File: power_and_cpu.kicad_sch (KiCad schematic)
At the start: 83 parts, among them J1 USB_C_Receptacle_USB2.0, J2 Conn_01x05, J3 Conn_01x05, J4 Conn_01x04, J5 Conn_01x04, J6 Conn_01x03, SW1 SW_MEC_5G, U11 RP2040, U13 ADC081S021CISD/NOPB, U14 ADC081S021CISD/NOPB, U15 ADC081S021CISD/NOPB, U16 ADC081S021CISD/NOPB, U6 NCP1117-3.3_SOT223, U7 XL7045, U9 W25Q16JVSSIQ, Y1 Crystal_GND24

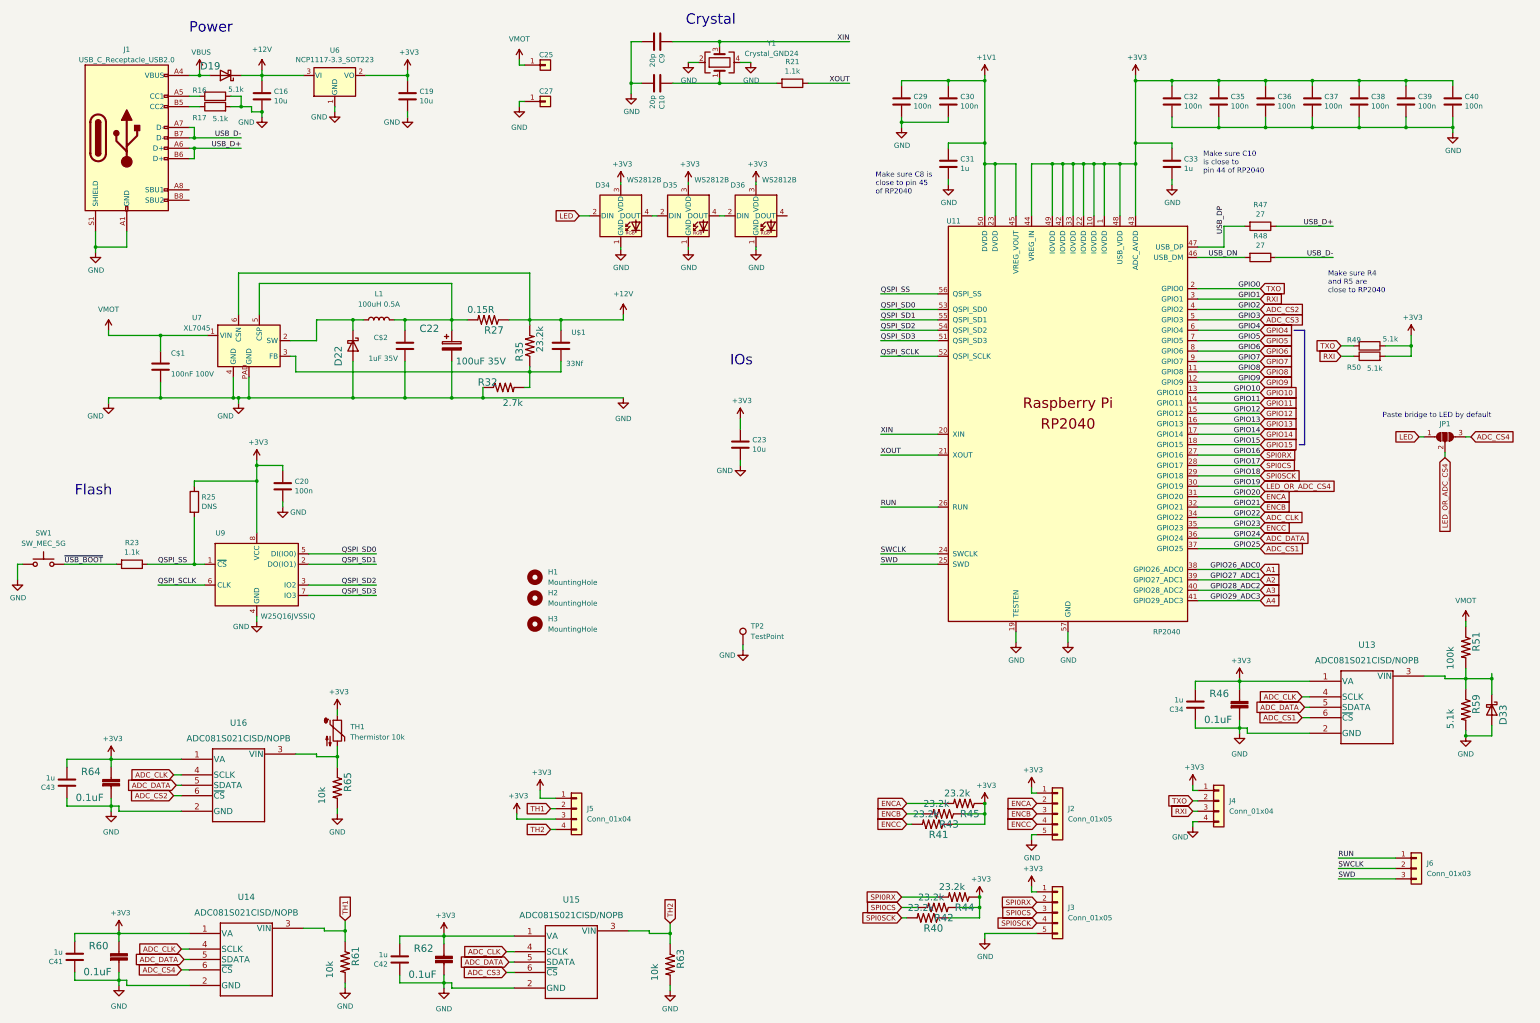
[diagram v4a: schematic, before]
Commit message: Additional updates to clean up power and capacitance on buck circuit.
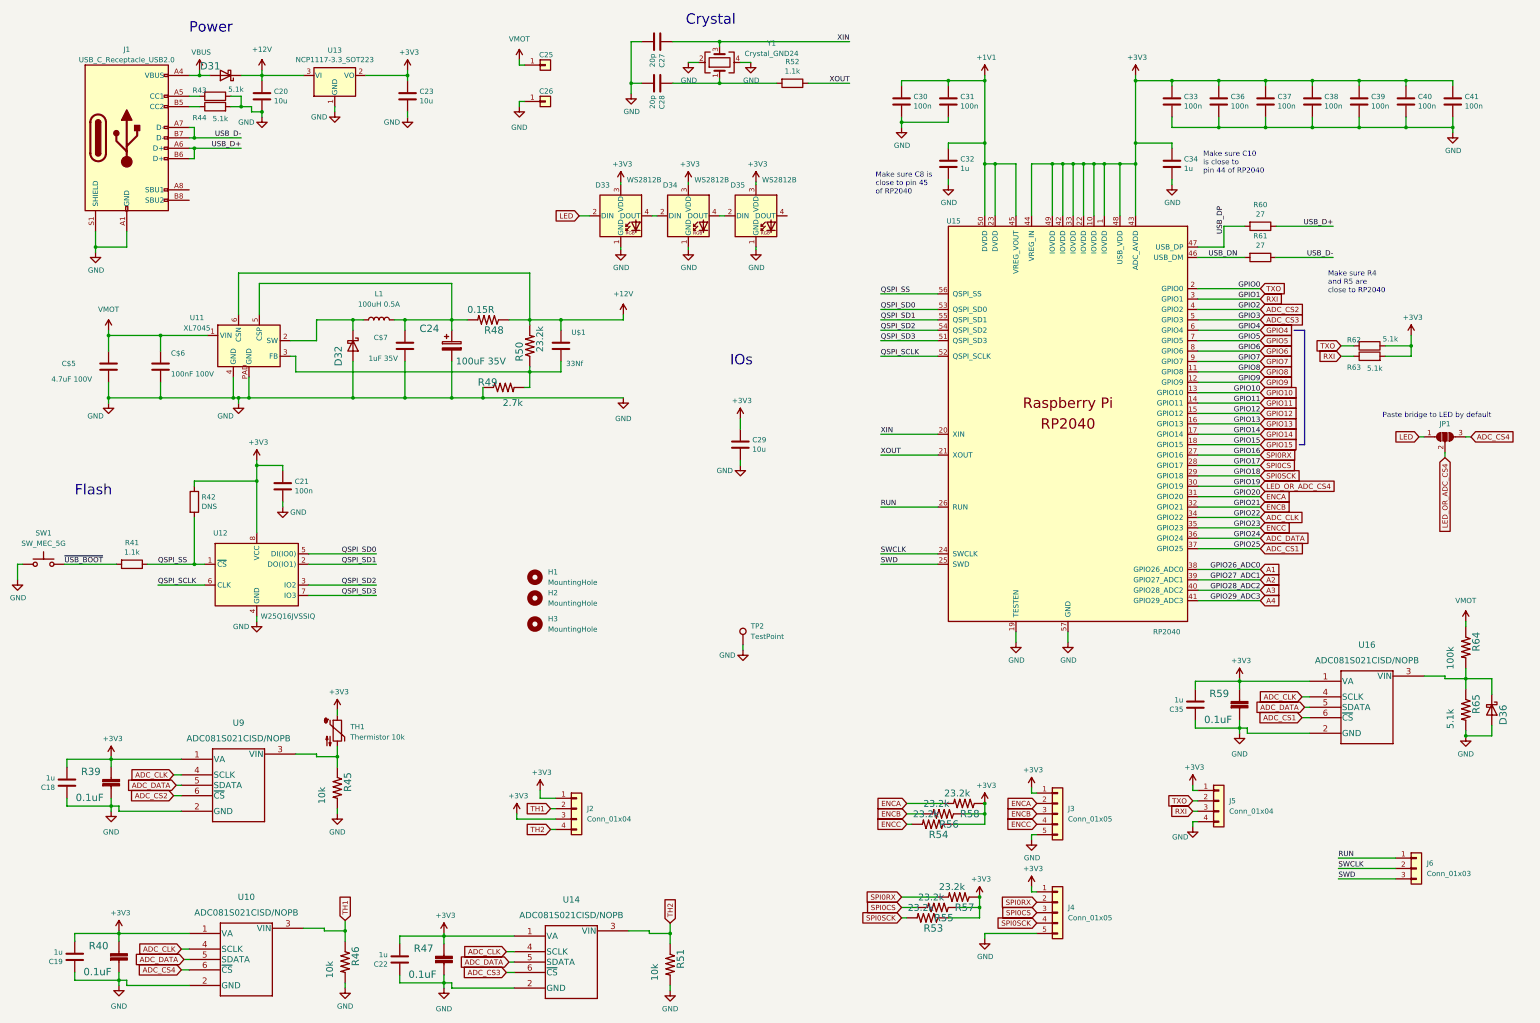
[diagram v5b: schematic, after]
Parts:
- added C$5: 4.7uF 100V, Capacitor_SMD:C_1210_3225Metric, symbol Device:C
- SW1: footprint Button_Switch_THT:SW_PUSH_6mm_H4.3mm -> parts:SW_TS_1101_C_W; LCSC C13828 -> C318938
- renumbered C$1 to C$6, C$2 to C$7, C43 to C18, C41 to C19, C16 to C20, C20 to C21, C42 to C22, C19 to C23, C22 to C24, C27 to C26, C9 to C27, C10 to C28, C23 to C29, C29 to C30, C30 to C31, C31 to C32, C32 to C33, C33 to C34, C34 to C35, C35 to C36, C36 to C37, C37 to C38, C38 to C39, C39 to C40, C40 to C41, D19 to D31, D22 to D32, D34 to D33, D35 to D34, D36 to D35, D33 to D36, J5 to J2, J2 to J3, J3 to J4, J4 to J5, R64 to R39, R60 to R40, R23 to R41, R25 to R42, R16 to R43, R17 to R44, R65 to R45, R61 to R46, R62 to R47, R27 to R48, R32 to R49, R35 to R50, R63 to R51, R21 to R52, R40 to R53, R41 to R54, R42 to R55, R43 to R56, R44 to R57, R45 to R58, R46 to R59, R47 to R60, R48 to R61, R49 to R62, R50 to R63, R51 to R64, R59 to R65, U14 to U10, U7 to U11, U9 to U12, U6 to U13, U15 to U14, U11 to U15, U13 to U16, U16 to U9
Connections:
- net GND: now also C$5.2
- net VMOT: now also C$5.1

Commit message: updated design with dual CPUs
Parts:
- removed D31: B5819W SL, Diode_SMD:D_SOD-123, symbol Diode:MBR340
- removed J5: Conn_01x04, Connector_Molex:Molex_KK-254_AE-6410-04A_1x04_P2.54mm_Vertical, symbol Connector_Generic:Conn_01x04
- removed J6: Conn_01x03, Connector_Molex:Molex_KK-254_AE-6410-03A_1x03_P2.54mm_Vertical, symbol Connector_Generic:Conn_01x03
- removed JP1: SolderJumper_3_Open, Jumper:SolderJumper-3_P1.3mm_Open_RoundedPad1.0x1.5mm_NumberLabels, symbol Jumper:SolderJumper_3_Open
- removed R40, R47: 0.1uF, Capacitor_SMD:C_0603_1608Metric, symbol MotorController:SPARKFUN-CAPACITORS_CAP
- removed U10, U14: ADC081S021CISD/NOPB, Package_TO_SOT_SMD:SOT-23-6, symbol 2022-06-16_01-48-54:ADC081S021CISD/NOPB
- removed U13: NCP1117-3.3_SOT223, Package_TO_SOT_SMD:SOT-223-3_TabPin2, symbol Regulator_Linear:NCP1117-3.3_SOT223
- added C42: 20p, Capacitor_SMD:C_0603_1608Metric, symbol Device:C
- added C43, C44, C45, C46, C47, C48, C49, C50, C51, C52, C56: 100n, Capacitor_SMD:C_0603_1608Metric, symbol Device:C
- added C53, C54: 1u, Capacitor_SMD:C_0603_1608Metric, symbol Device:C
- added C55: 100n, Capacitor_SMD:C_0603_1608Metric, symbol MotorController:SPARKFUN-CAPACITORS_CAP
- added C57, C58: 10p, Capacitor_SMD:C_0603_1608Metric, symbol Device:C
- added C60, C61, C62, C63, C64: 47p, Capacitor_SMD:C_0603_1608Metric, symbol Device:C
- added D37: B5819W SL, Diode_SMD:D_SOD-123, symbol Diode:MBR340
- added D38: LED_GREEN, LED_SMD:LED_0805_2012Metric, symbol Device:LED
- added D39: LED_ORANGE_RED, LED_SMD:LED_0805_2012Metric, symbol Device:LED
- added D40: CDSOT23-SM712, digikey-footprints:SOT-23-3, symbol odrive_aux_interface-rescue:CDSOT23-SM712-dk_TVS-Diodes
- added D41: LED_RED, LED_SMD:LED_0603_1608Metric, symbol Device:LED
- added H4: MountingHole, RP2040_minimal:MountingHole_3.9mm_Plastite_#6, symbol Mechanical:MountingHole
- added J10, J13, J14, J9: Conn_01x03, Connector_Molex:Molex_KK-254_AE-6410-03A_1x03_P2.54mm_Vertical, symbol Connector_Generic:Conn_01x03
- added J11: Conn_01x04, Connector_Molex:Molex_KK-254_AE-6410-04A_1x04_P2.54mm_Vertical, symbol Connector_Generic:Conn_01x04
- added J12, J5: Conn_01x06, Connector_Molex:Molex_KK-254_AE-6410-06A_1x06_P2.54mm_Vertical, symbol Connector_Generic:Conn_01x06
- added J15: Conn_01x05, Connector_Molex:Molex_KK-254_AE-6410-05A_1x05_P2.54mm_Vertical, symbol Connector_Generic:Conn_01x05
- added J6: USB_C_Receptacle_USB2.0, Connector_USB:USB_C_Receptacle_XKB_U262-16XN-4BVC11, symbol Connector:USB_C_Receptacle_USB2.0
- added J7: Conn_01x02, Connector_Molex:Molex_KK-254_AE-6410-02A_1x02_P2.54mm_Vertical, symbol Connector_Generic:Conn_01x02
- added J8: RJ45, Connector_RJ:RJ45_OST_PJ012-8P8CX_Vertical, symbol Connector:RJ45
- added R40, R46, R76: 5.1k, Resistor_SMD:R_0603_1608Metric, symbol Device:R
- added R47, R66: 1.1k, Resistor_SMD:R_0603_1608Metric, symbol Device:R
- added R51: DNS, Capacitor_SMD:C_0402_1005Metric, symbol Device:R
- added R67, R68: 1k, Resistor_SMD:R_0603_1608Metric, symbol Device:R
- added R70, R71: 27, Resistor_SMD:R_0603_1608Metric, symbol Device:R
- added R72: 10k, Resistor_SMD:R_0603_1608Metric, symbol MotorController:TAYLOR_RESISTOR
- added R75: 100R, Resistor_SMD:R_0603_1608Metric, symbol MotorController:TAYLOR_RESISTOR
- added R77: 68R, Resistor_SMD:R_0603_1608Metric, symbol MotorController:TAYLOR_RESISTOR
- added SW2: SW_MEC_5G, parts:SW_TS_1101_C_W, symbol Switch:SW_Push
- added U10: LD1086DT33TR, Package_TO_SOT_SMD:TO-252-2, symbol Regulator_Linear:LD1086DT33TR
- added U13: W25Q16JVSSIQ, Package_SO:SOIC-8_5.23x5.23mm_P1.27mm, symbol Memory_Flash:W25Q128JVS
- added U17: isolator, Package_SO:SOIC-8_7.5x5.85mm_P1.27mm, symbol Interface_CAN_LIN:ISO1050DUB
- added U18: MCP2515-xSO, Package_SO:SOIC-18W_7.5x11.6mm_P1.27mm, symbol Interface_CAN_LIN:MCP2515-xSO
- added U19: RP2040, RP2040_minimal:RP2040-QFN-56, symbol MCU_RaspberryPi_RP2040:RP2040
- added U21: EL357N(C)(TA)-G, Package_SO:SO-4_4.4x3.6mm_P2.54mm, symbol Isolator:LTV-357T
- added Y2, Y3: Crystal_GND24, Crystal:Crystal_SMD_3225-4Pin_3.2x2.5mm, symbol Device:Crystal_GND24
- C19: value 1u -> 20p; LCSC C15849 -> C1648
- C22: value 1u -> 10u; footprint Capacitor_SMD:C_0603_1608Metric -> Capacitor_SMD:C_0805_2012Metric; LCSC C15849 -> C15850
- C23: value 10u -> 47p; footprint Capacitor_SMD:C_0805_2012Metric -> Capacitor_SMD:C_0603_1608Metric; LCSC C15850 -> C1671
- J3, J4: LCSC C45012 -> C27544
- R39, R59: value 0.1uF -> 100n
- R53, R54, R55, R56, R57, R58: value 23.2k -> 10k; LCSC C23346 -> C25804
- renumbered C$7 to C72, U$1 to C73, C$6 to C74, C$5 to C75, R46 to R74, R51 to R79
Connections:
- net RUN is gone; now on net +3V3: U15.26 (RUN)
- net +12V: now also D37.1 (K), U10.3 (IN)
- net +1V1: now also C44.1, C45.1, C53.1, U19.23 (DVDD), U19.45 (VREG_VOUT), U19.50 (DVDD)
- net +3V3: now also C22.1, C43.1, C46.1, C47.1, C48.1, C49.1, C50.1, C51.1, C52.1, C54.1, C56.2, C60.1, C61.1, C62.1, C63.1, C64.1, D38.2 (A), D39.2 (A), J10.1 (Pin_1), J12.3 (Pin_3), J13.1 (Pin_1), J14.1 (Pin_1), J15.1 (Pin_1), J5.3 (Pin_3), J9.1 (Pin_1), R51.1, R72.2, R76.1, R77.1, U10.2 (OUT), U13.8 (VCC), U17.1 (VCC1), U18.18 (VDD), U19.1 (IOVDD), U19.10 (IOVDD), U19.22 (IOVDD), U19.26 (RUN), U19.33 (IOVDD), U19.42 (IOVDD), U19.43 (ADC_AVDD), U19.44 (VREG_IN), U19.48 (USB_VDD), U19.49 (IOVDD); no longer C19.2, C22.2
- net ADC_CLK: now also U19.4 (GPIO2); no longer U15.34 (GPIO22)
- net ADC_CS1: now also U19.7 (GPIO5); no longer U15.37 (GPIO25)
- net ADC_CS2: now also U19.3 (GPIO1); no longer U15.4 (GPIO2)
- net ADC_DATA: now also U19.2 (GPIO0); no longer U15.36 (GPIO24)
- net GND: now also C19.2, C22.2, C42.2, C43.2, C44.2, C45.2, C46.2, C47.2, C48.2, C49.2, C50.2, C51.2, C52.2, C53.2, C54.2, C56.1, C57.2, C58.2, D41.1 (K), J10.3 (Pin_3), J12.6 (Pin_6), J13.3 (Pin_3), J14.3 (Pin_3), J15.5 (Pin_5), J5.6 (Pin_6), J6.A1 (GND), J6.A12 (GND), J6.B1 (GND), J6.B12 (GND), J6.S1 (SHIELD), J9.3 (Pin_3), R40.1, R46.2, SW2.1, U10.1 (ADJ/GND), U13.4 (GND), U17.4 (GND1), U18.9 (VSS), U19.19 (TESTEN), U19.57 (GND), U21.3, Y2.2, Y2.4, Y3.2, Y3.4; no longer C19.1, C22.1, C23.2
- net LED: now also U19.18 (GPIO15)
- net RXI: now also U15.37 (GPIO25), J5.4 (Pin_4); no longer U15.3 (GPIO1)
- net SWCLK: now also J5.1 (Pin_1)
- net SWD: now also J5.2 (Pin_2)
- net TXO: now also U15.36 (GPIO24), J5.5 (Pin_5); no longer U15.2 (GPIO0)
- net VBUS: now also D37.2 (A), J6.A4 (VBUS), J6.A9 (VBUS), J6.B4 (VBUS), J6.B9 (VBUS)
- net ADC_CS3: no longer names the net of U15.5 (GPIO3)
- net ENCA renamed ENC1_RX
- net ENC1_RX: now also C62.2
- net ENCB renamed ENC1_CS
- net ENC1_CS: now also C61.2
- net ENCC renamed ENC1_SCK
- net ENC1_SCK: now also U15.34 (GPIO22), C60.2; no longer U15.35 (GPIO23)
- net LED_OR_ADC_CS4: no longer names the net of U15.30 (GPIO19)
- net SPI0CS renamed ENC2_CS
- net ENC2_CS: now also C63.2
- net SPI0RX renamed ENC2_RX
- net ENC2_RX: now also C64.2
- net SPI0SCK renamed ENC2_SCK
- net ENC2_SCK: now also C23.2
- net TH1 renamed A3_2
- net A3_2: now also U19.40 (GPIO28_ADC2)
- net TH2 renamed A4_2
- net A4_2: now also U19.41 (GPIO29_ADC3)
- new net: C58.1, U18.8 (OSC1), Y3.1
- new net: D41.2 (A), R77.2
- new net: D39.1 (K), R68.2
- new net: C57.1, U18.7 (OSC2), Y3.3
- new net: R75.2, U21.1
- new net: J6.A5 (CC1), R40.2
- new net: J6.B5 (CC2), R46.1
- new net: C42.1, R47.2, Y2.1
- new net: D38.1 (K), R67.2
- new net: R72.1, U18.17 (~{RESET})
- new net 5V_REMOTE: C55.2, J11.1 (Pin_1), J7.1 (Pin_1), J8.4, U17.8 (VCC2)
- new net A1_2: J9.2 (Pin_2), U19.38 (GPIO26_ADC0)
- new net A2_2: J13.2 (Pin_2), U19.39 (GPIO27_ADC1)
- new net AUX1: J10.2 (Pin_2), U19.8 (GPIO6)
- new net AUX2: J14.2 (Pin_2), U19.9 (GPIO7)
- new net AUX3_CSn: J15.3 (Pin_3), U19.32 (GPIO21)
- new net AUX3_RX: J15.2 (Pin_2), U19.31 (GPIO20)
- new net AUX3_SCK: J15.4 (Pin_4), U19.34 (GPIO22)
- new net CANH0: D40.2 (Input), J8.3, U17.7 (CANH)
- new net CANH1: J11.2 (Pin_2), J8.7
- new net CANL0: D40.1 (Input), J8.6, U17.6 (CANL)
- new net CANL1: J11.3 (Pin_3), J8.8
- new net ESTOP: R76.2, U19.17 (GPIO14), U21.4
- new net ESTOP_SQUARE: J8.1, R75.1
- new net ESTOP_SWITCH: J7.2 (Pin_2), J8.5
- new net GND_REMOTE: C55.1, D40.3 (Output), J11.4 (Pin_4), J8.2, U17.5 (GND2), U21.2
- new net QSPI_SCLK_2: U13.6 (CLK), U19.52 (QSPI_SCLK)
- new net QSPI_SD0_2: U13.5 (DI(IO0)), U19.53 (QSPI_SD0)
- new net QSPI_SD1_2: U13.2 (DO(IO1)), U19.55 (QSPI_SD1)
- new net QSPI_SD2_2: U13.3 (IO2), U19.54 (QSPI_SD2)
- new net QSPI_SD3_2: U13.7 (IO3), U19.51 (QSPI_SD3)
- new net QSPI_SS_2: R51.2, R66.1, U13.1 (~{CS}), U19.56 (QSPI_SS)
- new net RXD: R68.1, U17.2 (RXD), U18.2 (RXCAN)
- new net RXI_2: J12.4 (Pin_4), U19.37 (GPIO25)
- new net RXI_TX2: U15.3 (GPIO1), U19.15 (GPIO12)
- new net SPI1_CSn_2: U18.16 (~{CS}), U19.12 (GPIO9)
- new net SPI1_INT: U18.12 (~{INT}), U19.6 (GPIO4)
- new net SPI1_RX_2: U18.15 (SO), U19.11 (GPIO8)
- new net SPI1_SCK_2: U18.13 (SCK), U19.13 (GPIO10)
- new net SPI1_TX_2: U18.14 (SI), U19.14 (GPIO11)
- new net SWCLK_2: J12.1 (Pin_1), U19.24 (SWCLK)
- new net SWD_2: J12.2 (Pin_2), U19.25 (SWD)
- new net TXD: R67.1, U17.3 (TXD), U18.1 (TXCAN)
- new net TXO_2: J12.5 (Pin_5), U19.36 (GPIO24)
- new net TXO_RX2: U15.2 (GPIO0), U19.16 (GPIO13)
- new net USB_DN_2: R71.2, U19.46 (USB_DM)
- new net USB_DP_2: R70.2, U19.47 (USB_DP)
- new net USB_D_2+: J6.A6 (D+), J6.B6 (D+), R70.1
- new net USB_D_2-: J6.A7 (D-), J6.B7 (D-), R71.1
- new net XIN_2: C19.1, U19.20 (XIN), Y2.3
- new net XOUT_2: R47.1, U19.21 (XOUT)
- new net ~{USB_BOOT_2}: R66.2, SW2.2
- no-connect marks 0 -> 6
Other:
- note added: "Debug"
- note added: "PWR LED"
- note removed: "Paste bridge to LED by default"
- moved on the sheet: C35, D33, D34, D35, D36, J4, R53, R54, R55, R56, R57, R58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

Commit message: Updated design with Dual CPUs and improved current measurement
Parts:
- removed D36: DNS, Diode_SMD:D_SOD-523, symbol Diode:MBR340
- added C81: 10u, Capacitor_SMD:C_0805_2012Metric, symbol Device:C
- added D31: 1N4148WS, Diode_SMD:D_SOD-323, symbol Device:D
- added R9: 487R, Resistor_SMD:R_0603_1608Metric, symbol MotorController:TAYLOR_RESISTOR
- C55, R39, R59: symbol MotorController:SPARKFUN-CAPACITORS_CAP -> Device:C
- D40: LCSC C5122012 -> C521963
- J8: LCSC (none) -> C2902702
- R42, R51: footprint Capacitor_SMD:C_0402_1005Metric -> Resistor_SMD:R_0402_1005Metric
- U10: LCSC (none) -> C12051
- U11: footprint RP2040_minimal:SOIC-8_3.9x4.9mm_P1.27mm_POWERPAD -> Package_SO:SOIC-8-1EP_3.9x4.9mm_P1.27mm_EP2.41x3.81mm
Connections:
- net +3V3: now also C81.1, D31.1 (K)
- net CANH0: now also R9.1
- net CANL0: now also R9.2
- net GND: now also U11.9 (GND), C81.2; no longer U11.PAD (GND)
- net at R64.2, R65.1, U16.3 (VIN): now also D31.2 (A)
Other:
- moved on the sheet: D40

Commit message: Design that went to fab. Update controller design per design review.
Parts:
- added C86: 10u, Capacitor_SMD:C_0805_2012Metric, symbol Device:C
- added D36: CDSOT23-SM712, digikey-footprints:SOT-23-3, symbol odrive_aux_interface-rescue:CDSOT23-SM712-dk_TVS-Diodes
- added J16: RJ45, parts:RJ45_R-RJ45R08P-B000, symbol Connector:RJ45
- added J17, J18: Conn_02x04_Odd_Even, Connector_PinHeader_2.54mm:PinHeader_2x04_P2.54mm_Vertical, symbol Connector_Generic:Conn_02x04_Odd_Even
- added JP1, JP2: SolderJumper_2_Open, Jumper:SolderJumper-2_P1.3mm_Open_RoundedPad1.0x1.5mm, symbol Jumper:SolderJumper_2_Open
- added R10: 510R, Resistor_SMD:R_0603_1608Metric, symbol MotorController:TAYLOR_RESISTOR
- added TP1, TP3: TestPoint, TestPoint:TestPoint_Pad_1.0x1.0mm, symbol Connector:TestPoint
- added U23, U6: SN74LVC1G07QDCKTQ1, Package_TO_SOT_SMD:SOT-353_SC-70-5, symbol acorn-motherboard:SN74LVC1G07QDCKTQ1
- C57, C58: value 10p -> 18p; LCSC C106245 -> C1647
- D38: Digikey 160-1404-1-ND -> (none); MPN LTST-C150KGKT -> (none)
- D39: value LED_ORANGE_RED -> LED_YELLOW; Digikey 160-1404-1-ND -> 67-1696-1-ND; LCSC C72037 -> C5137318; MPN LTST-C150KGKT -> SML-LX1206SOC-TR
- J7: LCSC C29275 -> C27543
- J8: footprint Connector_RJ:RJ45_OST_PJ012-8P8CX_Vertical -> parts:RJ45_R-RJ45R08P-B000; LCSC C2902702 -> C386756
- R67: value 1k -> 27R; Digikey 311-1.00KCRCT-ND -> (none); LCSC C21190 -> C25190
- R68: value 1k -> 56R; Digikey 311-1.00KCRCT-ND -> (none); LCSC C21190 -> C25196
- R75: value 100R -> 120R; LCSC C105588 -> C22787
- R77: value 68R -> 82R; LCSC C17802 -> C23255
- R9: value 487R -> 120R; LCSC C2930108 -> C22787
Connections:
- net +1V1: no longer C44.1, C45.1, C53.1, U19.23 (DVDD), U19.45 (VREG_VOUT), U19.50 (DVDD)
- net +3V3: now also U23.5 (VCC), U6.5 (VCC); no longer D38.2 (A), D39.2 (A)
- net 5V_REMOTE: now also J16.4, J17.4 (Pin_4), J18.4 (Pin_4); no longer J7.1 (Pin_1)
- net CANH0: now also J16.3, J17.3 (Pin_3), J18.3 (Pin_3)
- net CANH1: now also D36.2 (Input), J16.7, J17.7 (Pin_7), J18.7 (Pin_7)
- net CANL0: now also J16.6, J17.6 (Pin_6), J18.6 (Pin_6), JP2.2 (B); no longer R9.2
- net CANL1: now also D36.1 (Input), J16.8, J17.8 (Pin_8), J18.8 (Pin_8)
- net ESTOP_SQUARE: now also J16.1, J17.1 (Pin_1), J18.1 (Pin_1)
- net GND: now also R67.1, R68.1, C86.2, U23.1 (/OE), U23.3 (GND), U6.1 (/OE), U6.3 (GND)
- net GND_REMOTE: now also C86.1, D36.3 (Output), J16.2, J17.2 (Pin_2), J18.2 (Pin_2), R10.2
- net RXD: now also TP3.1, U23.2 (A); no longer R68.1
- net TXD: now also TP1.1, U6.2 (A); no longer R67.1
- net ESTOP_SWITCH renamed ESTOP_SWITCH_IN
- net ESTOP_SWITCH_IN: now also J17.5 (Pin_5)
- new net: D38.2 (A), U6.4 (Y)
- new net: D39.2 (A), U23.4 (Y)
- new net: JP2.1 (A), R9.2
- new net: JP1.2 (B), R10.1
- new net 1V1_2: C44.1, C45.1, C53.1, U19.23 (DVDD), U19.45 (VREG_VOUT), U19.50 (DVDD)
- new net ESTOP_SWITCH_OUT: J16.5, J18.5 (Pin_5), J7.1 (Pin_1), JP1.1 (A)
- no-connect marks 6 -> 5
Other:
- moved on the sheet: C35, D31, D38, D40, J11, R59, R64, R65, R67, R68, U16
